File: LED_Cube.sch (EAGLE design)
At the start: 3 parts, among them IC1 MSGEQ7SOIC, U1 ATMEGA328P-AU, U2 TLC5940-RHB

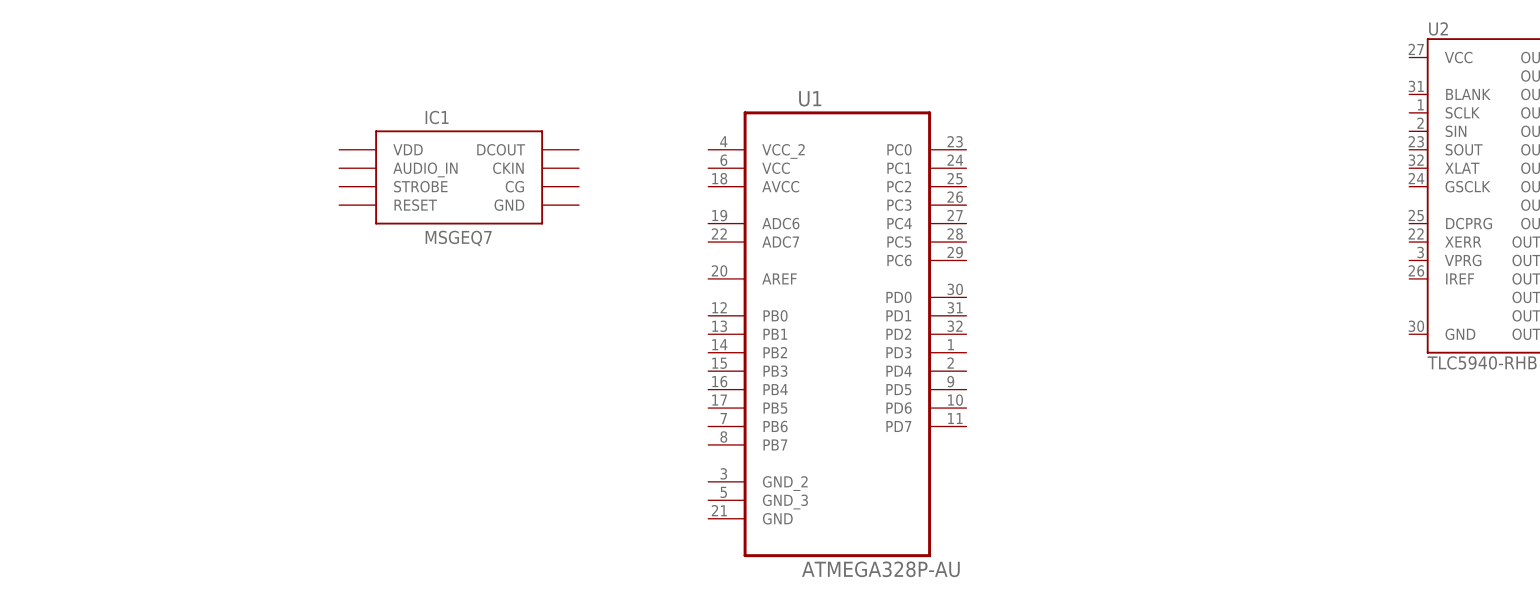
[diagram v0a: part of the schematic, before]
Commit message: MSGEQ7 Set up
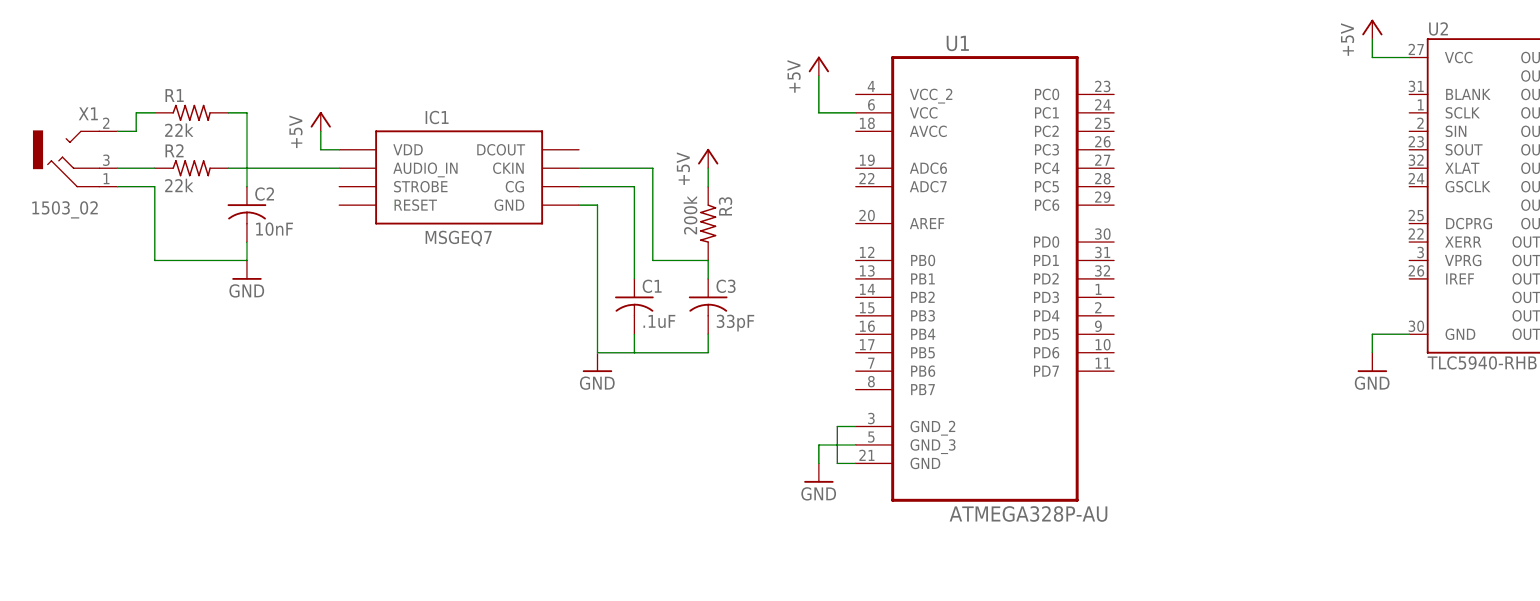
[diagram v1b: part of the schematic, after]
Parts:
- added C1: .1uF, rcl:C-USC0805
- added C2: 10nF, rcl:C-USC0805
- added C3: 33pF, rcl:C-USC0805
- added R1, R2: 22k, rcl:R-US_R0805
- added R3: 200k, rcl:R-US_R0805
- added X1: 1503_02, con-lumberg:1503_02
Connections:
- new net +5V: IC1.VDD, R3.1, U1.VCC, U2.VCC
- new net GND: C1.2, C2.2, C3.2, IC1.GND, U1.GND, U1.GND_2, U1.GND_3, U2.GND, X1.1
- new net N$1: R2.1, X1.3
- new net N$2: R1.1, X1.2
- new net N$3: C1.1, IC1.CG
- new net N$4: C3.1, IC1.CKIN
- new net N$6: C2.1, IC1.AUDIO_IN, R1.2, R2.2
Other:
- moved on the sheet: U1
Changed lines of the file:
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@@
 </layers>
 <schematic xreflabel="%F%N/%S.%C%R" xrefpart="/%S.%C%R">
+<description>ECE 411 LED Cube Practicum project</description>
 <attributes>
 </attributes>
@@
 <part name="IC1" library="msgeq7" deviceset="MSGEQ7" device="SOIC"/>
 <part name="U2" library="SparkFun-DigitalIC" deviceset="TLC5940" device="-RHB"/>
+<part name="GND1" library="supply1" deviceset="GND" device=""/>
+<part name="GND2" library="supply1" deviceset="GND" device=""/>
+<part name="GND3" library="supply1" deviceset="GND" device=""/>
+<part name="P+1" library="supply1" deviceset="+5V" device=""/>
+<part name="P+2" library="supply1" deviceset="+5V" device=""/>
+<part name="P+3" library="supply1" deviceset="+5V" device=""/>
+<part name="C1" library="rcl" deviceset="C-US" device="C0805" value=".1uF"/>
+<part name="C2" library="rcl" deviceset="C-US" device="C0805" value="10nF"/>
+<part name="X1" library="con-lumberg" deviceset="1503_02" device=""/>
+<part name="GND5" library="supply1" deviceset="GND" device=""/>
+<part name="R1" library="rcl" deviceset="R-US_" device="R0805" value="22k"/>
+<part name="R2" library="rcl" deviceset="R-US_" device="R0805" value="22k"/>
+<part name="R3" library="rcl" deviceset="R-US_" device="R0805" value="200k"/>
+<part name="C3" library="rcl" deviceset="C-US" device="C0805" value="33pF"/>
+<part name="P+4" library="supply1" deviceset="+5V" device=""/>
 </parts>
 <sheets>
@@
 </plain>
 <instances>
-<instance part="U1" gate="A" x="40.64" y="50.8"/>
+<instance part="U1" gate="A" x="60.96" y="58.42"/>
 <instance part="IC1" gate="G$1" x="-10.16" y="68.58"/>
 <instance part="U2" gate="G$1" x="132.08" y="68.58"/>
+<instance part="GND1" gate="1" x="7.62" y="43.18"/>
+<instance part="GND2" gate="1" x="38.1" y="27.94"/>
+<instance part="GND3" gate="1" x="114.3" y="43.18"/>
+<instance part="P+1" gate="1" x="-30.48" y="78.74"/>
+<instance part="P+2" gate="1" x="38.1" y="86.36"/>
+<instance part="P+3" gate="1" x="114.3" y="91.44"/>
+<instance part="C1" gate="G$1" x="12.7" y="53.34"/>
+<instance part="C2" gate="G$1" x="-40.64" y="66.04"/>
+<instance part="X1" gate="G$1" x="-63.5" y="73.66" rot="MR0"/>
+<instance part="GND5" gate="1" x="-40.64" y="55.88"/>
+<instance part="R1" gate="G$1" x="-48.26" y="78.74"/>
+<instance part="R2" gate="G$1" x="-48.26" y="71.12"/>
+<instance part="R3" gate="G$1" x="22.86" y="63.5" rot="R270"/>
+<instance part="C3" gate="G$1" x="22.86" y="53.34"/>
+<instance part="P+4" gate="1" x="22.86" y="73.66"/>
 </instances>
 <busses>
 </busses>
 <nets>
+<net name="+5V" class="0">
+<segment>
+<pinref part="IC1" gate="G$1" pin="VDD"/>
+<pinref part="P+1" gate="1" pin="+5V"/>
+<wire x1="-27.94" y1="73.66" x2="-30.48" y2="73.66" width="0.1524" layer="91"/>
+<wire x1="-30.48" y1="73.66" x2="-30.48" y2="76.2" width="0.1524" layer="91"/>
+</segment>
+<segment>
+<pinref part="U2" gate="G$1" pin="VCC"/>
+<pinref part="P+3" gate="1" pin="+5V"/>
+<wire x1="119.38" y1="86.36" x2="114.3" y2="86.36" width="0.1524" layer="91"/>
+<wire x1="114.3" y1="86.36" x2="114.3" y2="88.9" width="0.1524" layer="91"/>
+</segment>
+<segment>
+<pinref part="U1" gate="A" pin="VCC"/>
+<pinref part="P+2" gate="1" pin="+5V"/>
+<wire x1="43.18" y1="78.74" x2="38.1" y2="78.74" width="0.1524" layer="91"/>
+<wire x1="38.1" y1="78.74" x2="38.1" y2="83.82" width="0.1524" layer="91"/>
+</segment>
+<segment>
+<pinref part="R3" gate="G$1" pin="1"/>
+<pinref part="P+4" gate="1" pin="+5V"/>
+<wire x1="22.86" y1="68.58" x2="22.86" y2="71.12" width="0.1524" layer="91"/>
+</segment>
+</net>
+<net name="GND" class="0">
+<segment>
+<pinref part="IC1" gate="G$1" pin="GND"/>
+<pinref part="GND1" gate="1" pin="GND"/>
+<wire x1="5.08" y1="66.04" x2="7.62" y2="66.04" width="0.1524" layer="91"/>
+<wire x1="7.62" y1="66.04" x2="7.62" y2="45.72" width="0.1524" layer="91"/>
+<pinref part="C1" gate="G$1" pin="2"/>
+<wire x1="12.7" y1="48.26" x2="12.7" y2="45.72" width="0.1524" layer="91"/>
+<wire x1="12.7" y1="45.72" x2="7.62" y2="45.72" width="0.1524" layer="91"/>
+<pinref part="C3" gate="G$1" pin="2"/>
+<wire x1="22.86" y1="48.26" x2="22.86" y2="45.72" width="0.1524" layer="91"/>
+<wire x1="22.86" y1="45.72" x2="12.7" y2="45.72" width="0.1524" layer="91"/>
+</segment>
+<segment>
+<pinref part="U1" gate="A" pin="GND"/>
+<wire x1="43.18" y1="30.48" x2="40.64" y2="30.48" width="0.1524" layer="91"/>
+<wire x1="40.64" y1="30.48" x2="40.64" y2="33.02" width="0.1524" layer="91"/>
+<pinref part="U1" gate="A" pin="GND_3"/>
+<wire x1="40.64" y1="33.02" x2="43.18" y2="33.02" width="0.1524" layer="91"/>
+<pinref part="U1" gate="A" pin="GND_2"/>
+<wire x1="43.18" y1="35.56" x2="40.64" y2="35.56" width="0.1524" layer="91"/>
+<wire x1="40.64" y1="35.56" x2="40.64" y2="33.02" width="0.1524" layer="91"/>
+<pinref part="GND2" gate="1" pin="GND"/>
+<wire x1="40.64" y1="33.02" x2="38.1" y2="33.02" width="0.1524" layer="91"/>
+<wire x1="38.1" y1="33.02" x2="38.1" y2="30.48" width="0.1524" layer="91"/>
+</segment>
+<segment>
+<pinref part="U2" gate="G$1" pin="GND"/>
+<pinref part="GND3" gate="1" pin="GND"/>
+<wire x1="119.38" y1="48.26" x2="114.3" y2="48.26" width="0.1524" layer="91"/>
+<wire x1="114.3" y1="48.26" x2="114.3" y2="45.72" width="0.1524" layer="91"/>
+</segment>
+<segment>
+<pinref part="GND5" gate="1" pin="GND"/>
+<pinref part="C2" gate="G$1" pin="2"/>
+<wire x1="-40.64" y1="58.42" x2="-40.64" y2="60.96" width="0.1524" layer="91"/>
+<pinref part="X1" gate="G$1" pin="1"/>
+<wire x1="-58.42" y1="68.58" x2="-53.34" y2="68.58" width="0.1524" layer="91"/>
+<wire x1="-53.34" y1="68.58" x2="-53.34" y2="58.42" width="0.1524" layer="91"/>
+<wire x1="-53.34" y1="58.42" x2="-40.64" y2="58.42" width="0.1524" layer="91"/>
+</segment>
+</net>
+<net name="N$6" class="0">
+<segment>
+<pinref part="IC1" gate="G$1" pin="AUDIO_IN"/>
+<wire x1="-27.94" y1="71.12" x2="-40.64" y2="71.12" width="0.1524" layer="91"/>
+<pinref part="C2" gate="G$1" pin="1"/>
+<wire x1="-40.64" y1="71.12" x2="-40.64" y2="78.74" width="0.1524" layer="91"/>
+<wire x1="-40.64" y1="68.58" x2="-40.64" y2="71.12" width="0.1524" layer="91"/>
+<pinref part="R2" gate="G$1" pin="2"/>
+<wire x1="-43.18" y1="71.12" x2="-40.64" y2="71.12" width="0.1524" layer="91"/>
+<pinref part="R1" gate="G$1" pin="2"/>
+<wire x1="-40.64" y1="78.74" x2="-43.18" y2="78.74" width="0.1524" layer="91"/>
+</segment>
+</net>
+<net name="N$1" class="0">
+<segment>
+<pinref part="X1" gate="G$1" pin="3"/>
+<pinref part="R2" gate="G$1" pin="1"/>
+<wire x1="-58.42" y1="71.12" x2="-53.34" y2="71.12" width="0.1524" layer="91"/>
+</segment>
+</net>
+<net name="N$4" class="0">
+<segment>
+<pinref part="IC1" gate="G$1" pin="CKIN"/>
+<wire x1="5.08" y1="71.12" x2="15.24" y2="71.12" width="0.1524" layer="91"/>
+<wire x1="15.24" y1="71.12" x2="15.24" y2="58.42" width="0.1524" layer="91"/>
+<pinref part="C3" gate="G$1" pin="1"/>
+<wire x1="15.24" y1="58.42" x2="22.86" y2="58.42" width="0.1524" layer="91"/>
+<wire x1="22.86" y1="58.42" x2="22.86" y2="55.88" width="0.1524" layer="91"/>
+</segment>
+</net>
+<net name="N$2" class="0">
+<segment>
+<pinref part="X1" gate="G$1" pin="2"/>
+<wire x1="-58.42" y1="76.2" x2="-55.88" y2="76.2" width="0.1524" layer="91"/>
+<wire x1="-55.88" y1="76.2" x2="-55.88" y2="78.74" width="0.1524" layer="91"/>
+<pinref part="R1" gate="G$1" pin="1"/>
+<wire x1="-55.88" y1="78.74" x2="-53.34" y2="78.74" width="0.1524" layer="91"/>
+</segment>
+</net>
+<net name="N$3" class="0">
+<segment>
+<pinref part="C1" gate="G$1" pin="1"/>
+<wire x1="12.7" y1="55.88" x2="12.7" y2="68.58" width="0.1524" layer="91"/>
+<pinref part="IC1" gate="G$1" pin="CG"/>
+<wire x1="12.7" y1="68.58" x2="5.08" y2="68.58" width="0.1524" layer="91"/>
+</segment>
+</net>
 </nets>
 </sheet>

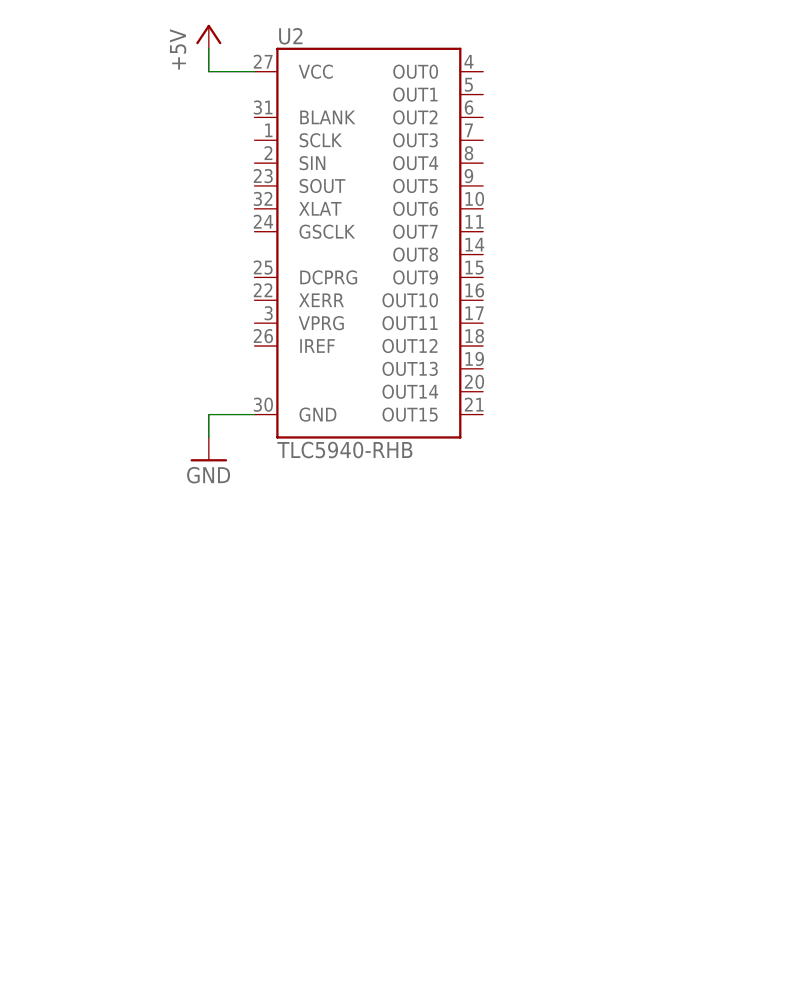
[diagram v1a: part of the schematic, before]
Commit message: 1/3 TLC5940 set up
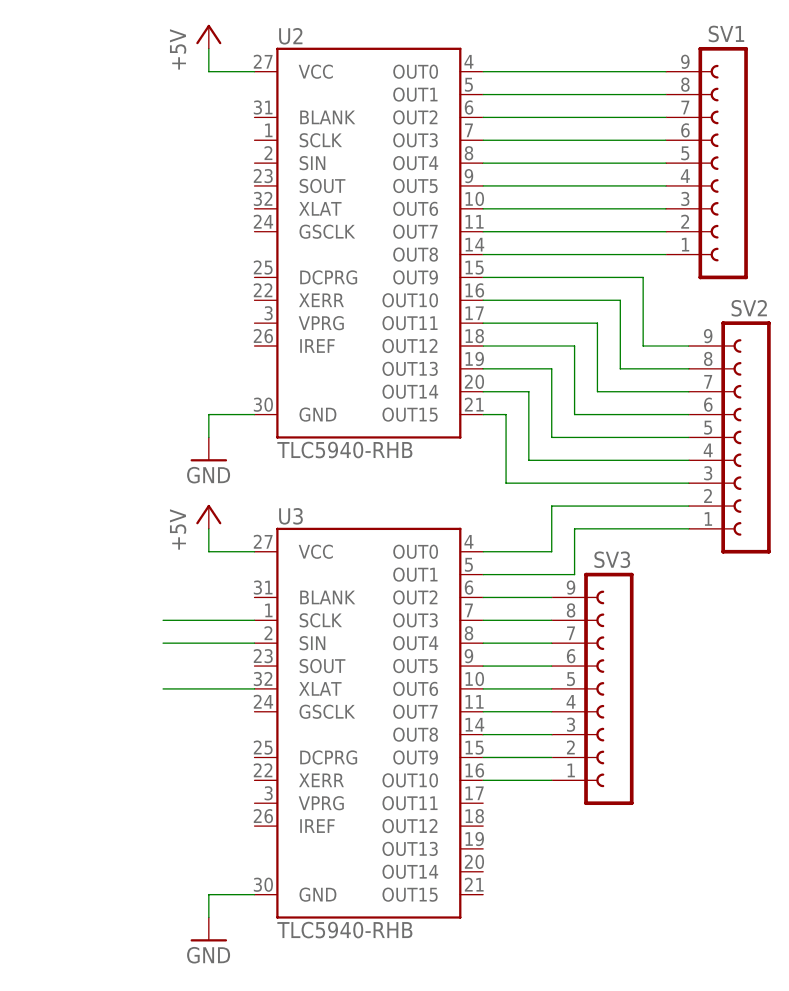
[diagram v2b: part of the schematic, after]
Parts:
- added SV1, SV2, SV3: (no value), con-lsta:FE09-1
- added U3: TLC5940-RHB, SparkFun-DigitalIC:TLC5940-RHB
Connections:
- new net N$10: SV1.5, U2.OUT4
- new net N$11: SV1.4, U2.OUT5
- new net N$12: SV1.3, U2.OUT6
- new net N$13: SV1.2, U2.OUT7
- new net N$14: SV3.1, U3.OUT10
- new net N$15: SV1.1, U2.OUT8
- new net N$16: SV3.2, U3.OUT9
- new net N$17: SV3.3, U3.OUT8
- new net N$18: SV3.4, U3.OUT7
- new net N$19: SV3.5, U3.OUT6
- new net N$20: SV3.6, U3.OUT5
- new net N$21: SV3.7, U3.OUT4
- new net N$22: SV3.8, U3.OUT3
- new net N$23: SV3.9, U3.OUT2
- new net N$24: SV2.1, U3.OUT1
- new net N$25: SV2.2, U3.OUT0
- new net N$26: SV2.9, U2.OUT9
- new net N$27: SV2.8, U2.OUT10
- new net N$28: SV2.7, U2.OUT11
- new net N$29: SV2.6, U2.OUT12
- new net N$30: SV2.5, U2.OUT13
- new net N$31: SV2.4, U2.OUT14
- new net N$32: SV2.3, U2.OUT15
- new net N$33: U3.SCLK
- new net N$34: U3.SIN
- new net N$35: U3.XLAT
- new net N$5: SV1.6, U2.OUT3
- new net N$7: SV1.9, U2.OUT0
- new net N$8: SV1.8, U2.OUT1
- new net N$9: SV1.7, U2.OUT2
- net +5V: now also U3.VCC
- net GND: now also U3.GND

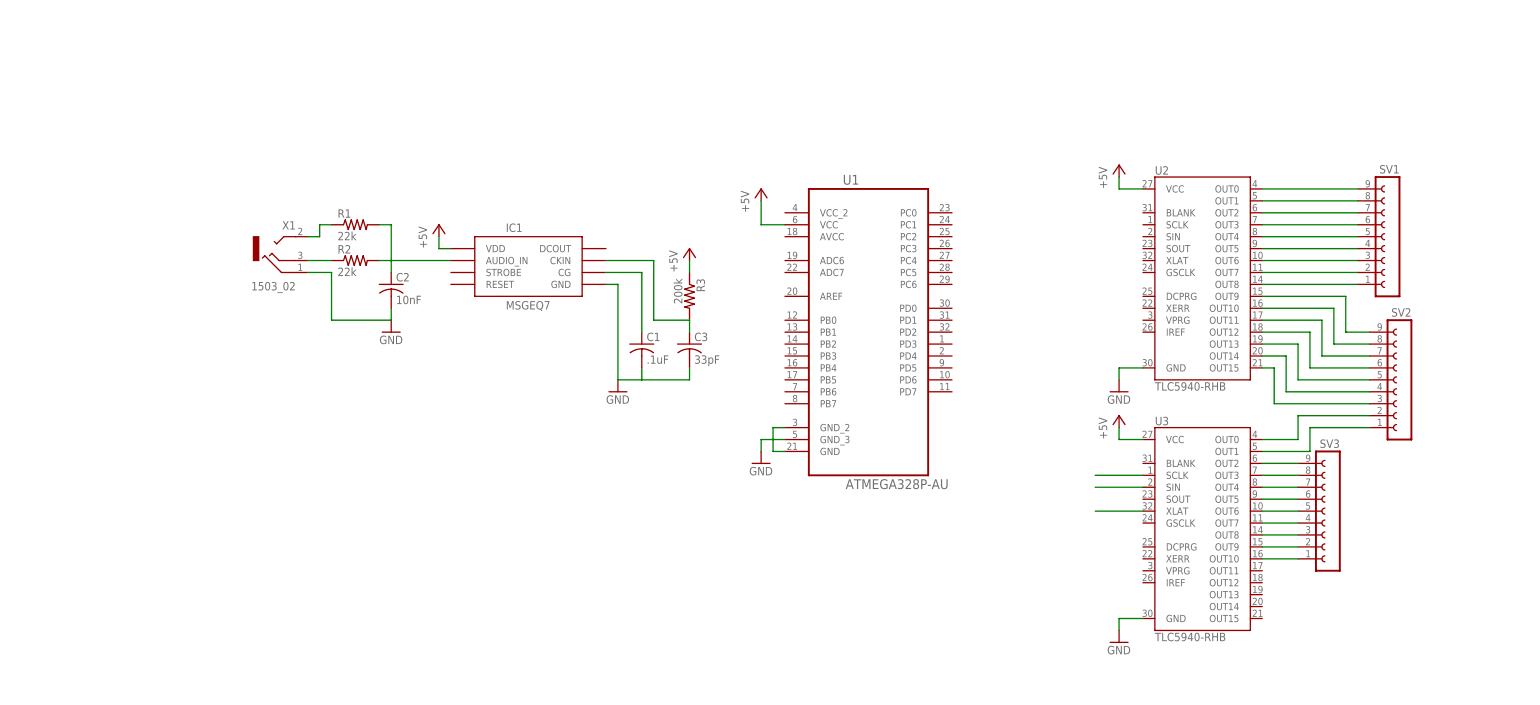
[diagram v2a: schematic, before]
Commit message: began ATMEGA integration into schemaic. Specified tenative pins
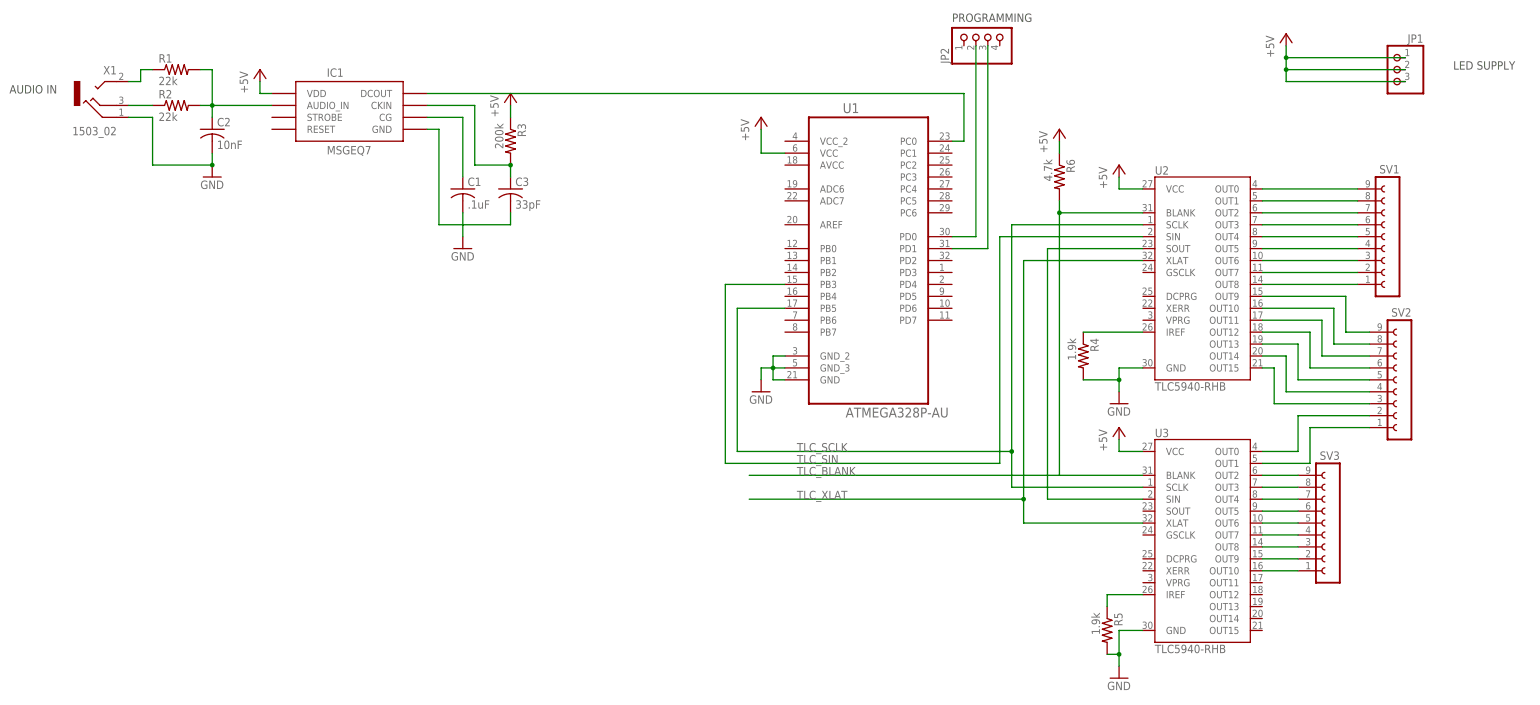
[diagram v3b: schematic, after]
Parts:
- added JP1: (no value), pinhead:PINHD-1X3
- added JP2: (no value), pinhead:PINHD-1X4
- added R4, R5: 1.9k, rcl:R-US_R0805
- added R6: 4.7k, rcl:R-US_R0805
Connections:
- new net N$36: IC1.DCOUT, U1.PC0
- new net N$39: R5.1, U3.IREF
- new net N$40: R4.1, U2.IREF
- new net TLC_BLANK: R6.2, U2.BLANK, U3.BLANK
- new net TLC_SCLK: U1.PB5, U2.SCLK, U3.SCLK
- new net TLC_SIN: U1.PB3, U2.SIN
- new net TLC_XLAT: U2.XLAT, U3.XLAT
- net +5V: now also JP1.1, JP1.2, JP1.3, R6.1
- net GND: now also R4.2, R5.2
- net N$33: now also JP2.2, U1.PD0; no longer U3.SCLK
- net N$34: now also U2.SOUT
- net N$35: now also JP2.3, U1.PD1; no longer U3.XLAT
- net N$4: now also R3.2
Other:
- note added: "AUDIO IN"
- note added: "LED SUPPLY"
- note added: "PROGRAMMING"
- moved on the sheet: C1, C2, C3, IC1, R1, R2, R3, SV3, U1, U3, X1
